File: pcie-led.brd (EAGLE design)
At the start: 74.6 x 50.8 mm, 64 parts, among them IC1 LED6001, IC2 LM556D, IC3 NL27WZ07, J1 45558-0003, J2 15-24-4441, Q1 BSC340N08NS3G, Q2 BSC340N08NS3G

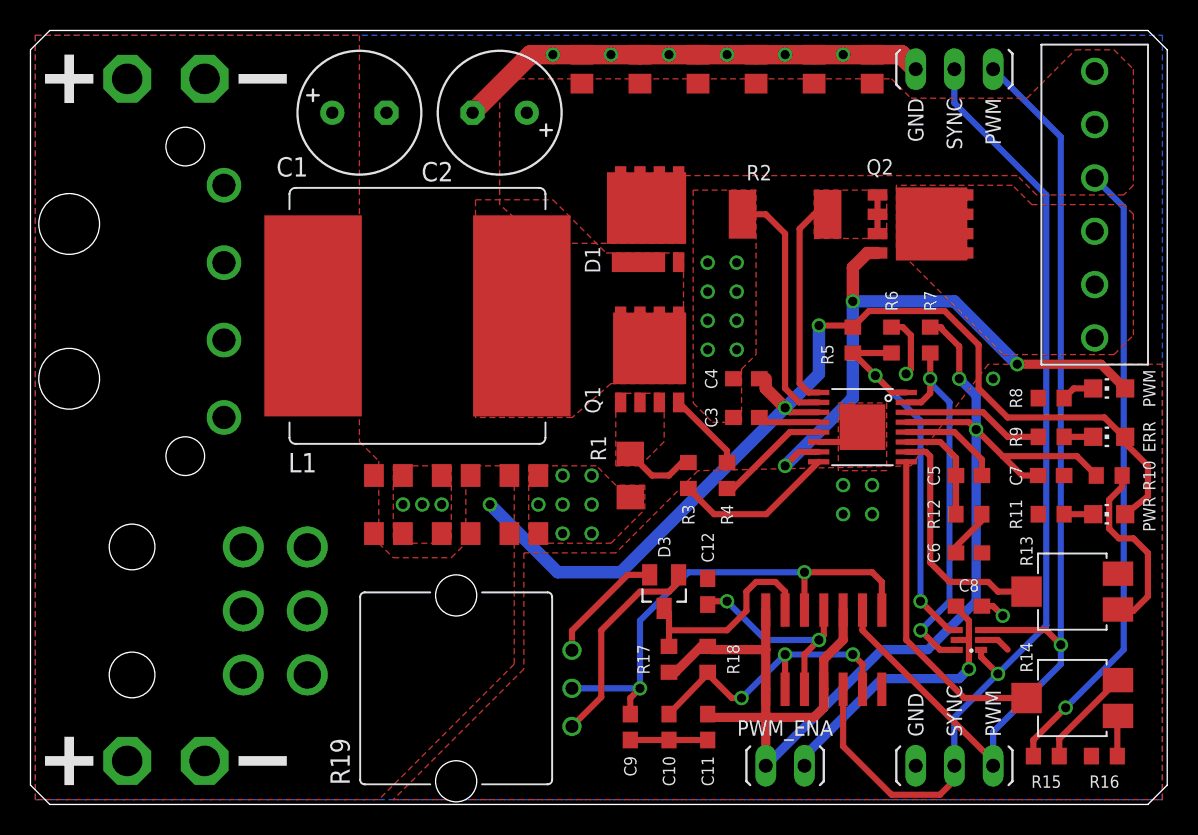
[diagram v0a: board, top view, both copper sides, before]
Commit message: Fix errors with clock and PWM generators
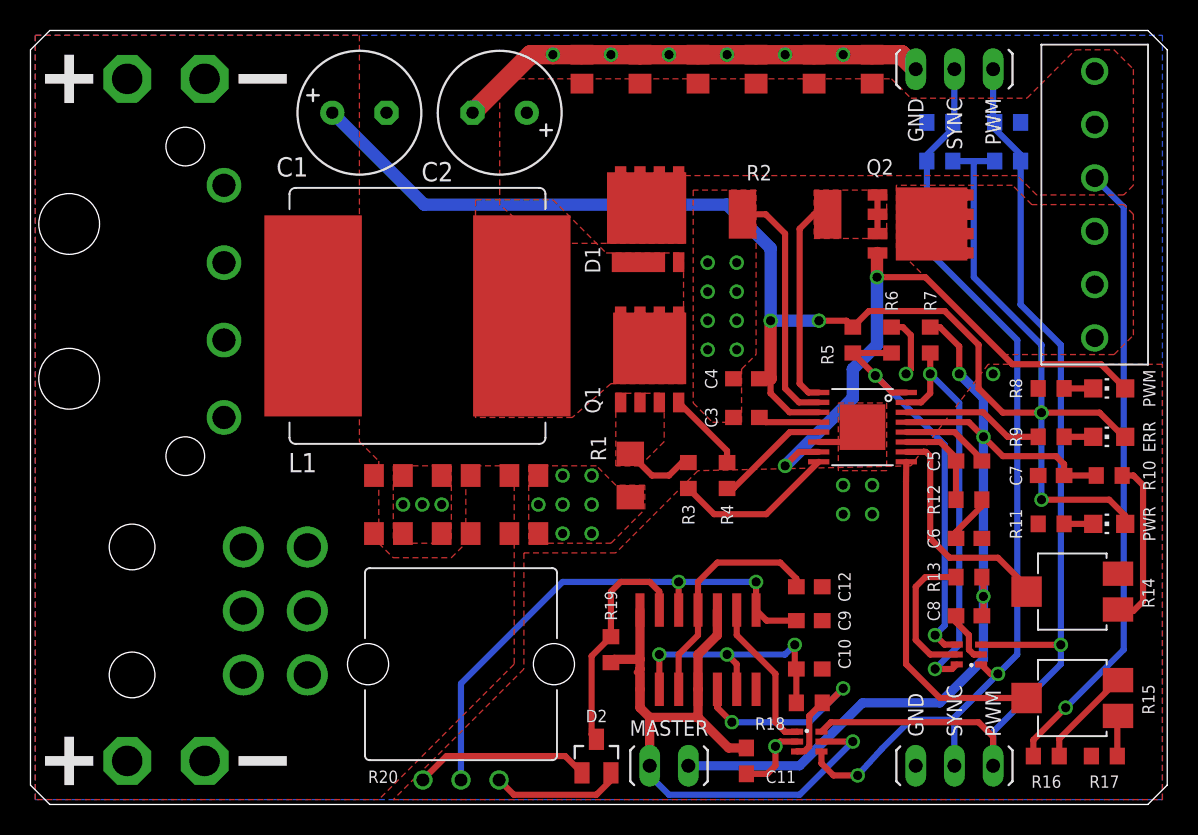
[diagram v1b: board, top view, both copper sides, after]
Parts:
- removed D3: BAS40-04, diode:SOT23
- removed PWM_ENA: (no value), parts:JP1
- added D2: BAS40-04, diode:SOT23
- added IC4: NL27WZ07, parts:SOT363
- added MASTER: (no value), parts:JP1
- added R20: 100k, parts:P260T
- added R21, R22: 100k, resistor:R0603
- added R23, R24: 39k, resistor:R0603
- C2A, C2B, C2C, C2D, C2E, C2F: value 2.2uF -> 0.47uF
- R13: value 5k -> 0; device parts:ST-4EB -> resistor:R0603
- R15: value 160k -> 5k; device resistor:R0603 -> parts:ST-4EB
- R16: value 2.2k -> 160k
- R17: value 10k -> 2.2k
- R19: value 100k -> 10k; device parts:P260T -> resistor:R0603
- R5, R7: value 50k -> 100k
- R6: value 10k -> 39k
- moved R17 29.3 mm to (70.5, 3.17), turned to 0 degrees
- moved C9 13.7 mm to (51.1, 12.1), turned to 0 degrees
- moved R19 10.5 mm to (38.1, 10.2), turned to 270 degrees
- moved C10 9.96 mm to (51.1, 8.89), turned to 0 degrees
- moved IC2 8.26 mm to (43.8, 10.2)
- moved R18 7.25 mm to (51.1, 6.67), turned to 0 degrees
- moved R13 7.05 mm to (61.6, 14.9)
- moved R14 6.99 mm to (68.6, 14.0)
- moved C12 6.68 mm to (51.1, 14.3), turned to 0 degrees
- moved R15 4.26 mm to (68.6, 6.99), turned to 0 degrees
- moved R16 3.81 mm to (66.7, 3.17), turned to 180 degrees
- moved C11 3.38 mm to (47.0, 2.86)
- moved C5 0.95 mm to (61.6, 22.5)
- moved IC3 0.95 mm to (61.6, 9.84)
- moved R12 0.95 mm to (61.6, 20.0)
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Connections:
- new net N$16: IC3.5, R13.1
- new net N$6: IC2.5, IC4.3, R18.2
- new net N$8: IC2.9, IC4.1
- net +12V: now also R21.1, R22.1
- net +3V3: now also C8.1, MASTER.2, R13.2; no longer C11.1, IC2.1, IC2.10, IC2.14, IC2.4, PWM_ENA.2, R17.2, R18.1
- net EXTPWM: now also IC4.6, R22.2, R24.1; no longer IC2.9
- net EXTSYNC: now also IC4.4, R21.2, R23.1; no longer IC2.5
- net GND: now also IC4.2, R14.1, R17.1, R23.2, R24.2; no longer R13.1, R16.1
- net LED+: now also R16.2; no longer R15.2
- net N$11: now also R15.2; no longer R14.2
- net N$12: now also R14.2; no longer R13.2
- net N$13: now also R15.3, R17.2; no longer R14.3, R16.2
- net N$14: now also R14.3; no longer R13.3
- net N$21: now also R18.1; no longer R18.2
- net N$23: now also D2.2, R20.3; no longer D3.2, R19.3
- net N$24: now also D2.1, R20.1; no longer D3.1, R19.1
- net N$25: now also R20.2; no longer R19.2
- net N$26: now also D2.3, R19.1; no longer D3.3, R17.1
- net N$4: now also C11.1, IC2.1, IC2.10, IC2.14, IC2.4, IC4.5, MASTER.1, R19.2; no longer C8.1, IC3.5, PWM_ENA.1
- net N$7: now also R16.1; no longer R14.1
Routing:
- net +12V: track 72.9 -> 112.7 mm, vias 3 -> 4
- net N$4: track 19.1 -> 46.0 mm
- net +3V3: track 87.3 -> 63.1 mm, vias 2 -> 3
- net N$6: track 0.00 -> 16.7 mm, vias 0 -> 2
- net N$8: track 0.00 -> 10.1 mm
- net N$16: track 0.00 -> 9.49 mm
- net N$25: track 32.6 -> 35.1 mm
- net N$24: track 14.0 -> 11.6 mm
- net N$21: track 20.0 -> 17.8 mm
- net EXTSYNC: track 66.5 -> 64.4 mm, vias 1 -> 2
- net PWMI: track 26.3 -> 28.0 mm
- net FSW: track 25.2 -> 26.8 mm
- net N$26: track 13.8 -> 15.3 mm
- net N$18: track 14.2 -> 15.5 mm, vias 2 -> 0
- net N$2: track 39.7 -> 38.4 mm, vias 3 -> 2
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
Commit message: Tweaks for DRC, and shrink board <5cm width
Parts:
- moved R21 7.36 mm to (60.6, 34.9), turned to 90 degrees
- moved R22 7.31 mm to (64.5, 34.9), turned to 90 degrees
- moved R23 5.48 mm to (60.6, 39.4), turned to 270 degrees
- moved R24 5.41 mm to (64.5, 39.4), turned to 90 degrees
- moved IC3 1.59 mm to (61.6, 8.26)
- moved C1 1.27 mm to (21.6, 44.1)
- moved C2 1.27 mm to (30.8, 44.1)
- moved L1 1.27 mm to (25.4, 30.8)
- moved Q2 1.27 mm to (58.4, 36.8)
- moved D2 1.27 mm to (37.1, 4.45)
- moved C1A 1.27 mm to (23.5, 20.3)
- moved C1C 1.27 mm to (27.9, 20.3)
- moved C1E 1.27 mm to (32.4, 20.3)
- moved C3 1.27 mm to (47.0, 24.1)
- moved C4 1.27 mm to (47.0, 26.7)
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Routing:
- net +12V: track 112.7 -> 105.8 mm
- net N$4: track 46.0 -> 42.8 mm
- net EXTSYNC: track 64.4 -> 67.0 mm
- net N$7: track 6.58 -> 8.12 mm
- net N$26: track 15.3 -> 14.0 mm
- net LED+: track 41.2 -> 40.1 mm
- net EXTPWM: track 68.8 -> 69.5 mm
- net N$14: track 11.2 -> 11.8 mm
- net +3V3: track 63.1 -> 62.6 mm
- net GND: track 68.8 -> 69.1 mm, vias 31 -> 30
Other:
- board size 74.6 x 50.8 mm -> 74.6 x 49.5 mm
